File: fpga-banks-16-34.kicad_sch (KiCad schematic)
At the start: 20 parts, among them U3002 XC7K160T-FFG676, U9001 Oscillator_SMD_100MHz_ASFLMB, U9002 PCA9517A_TSSOP

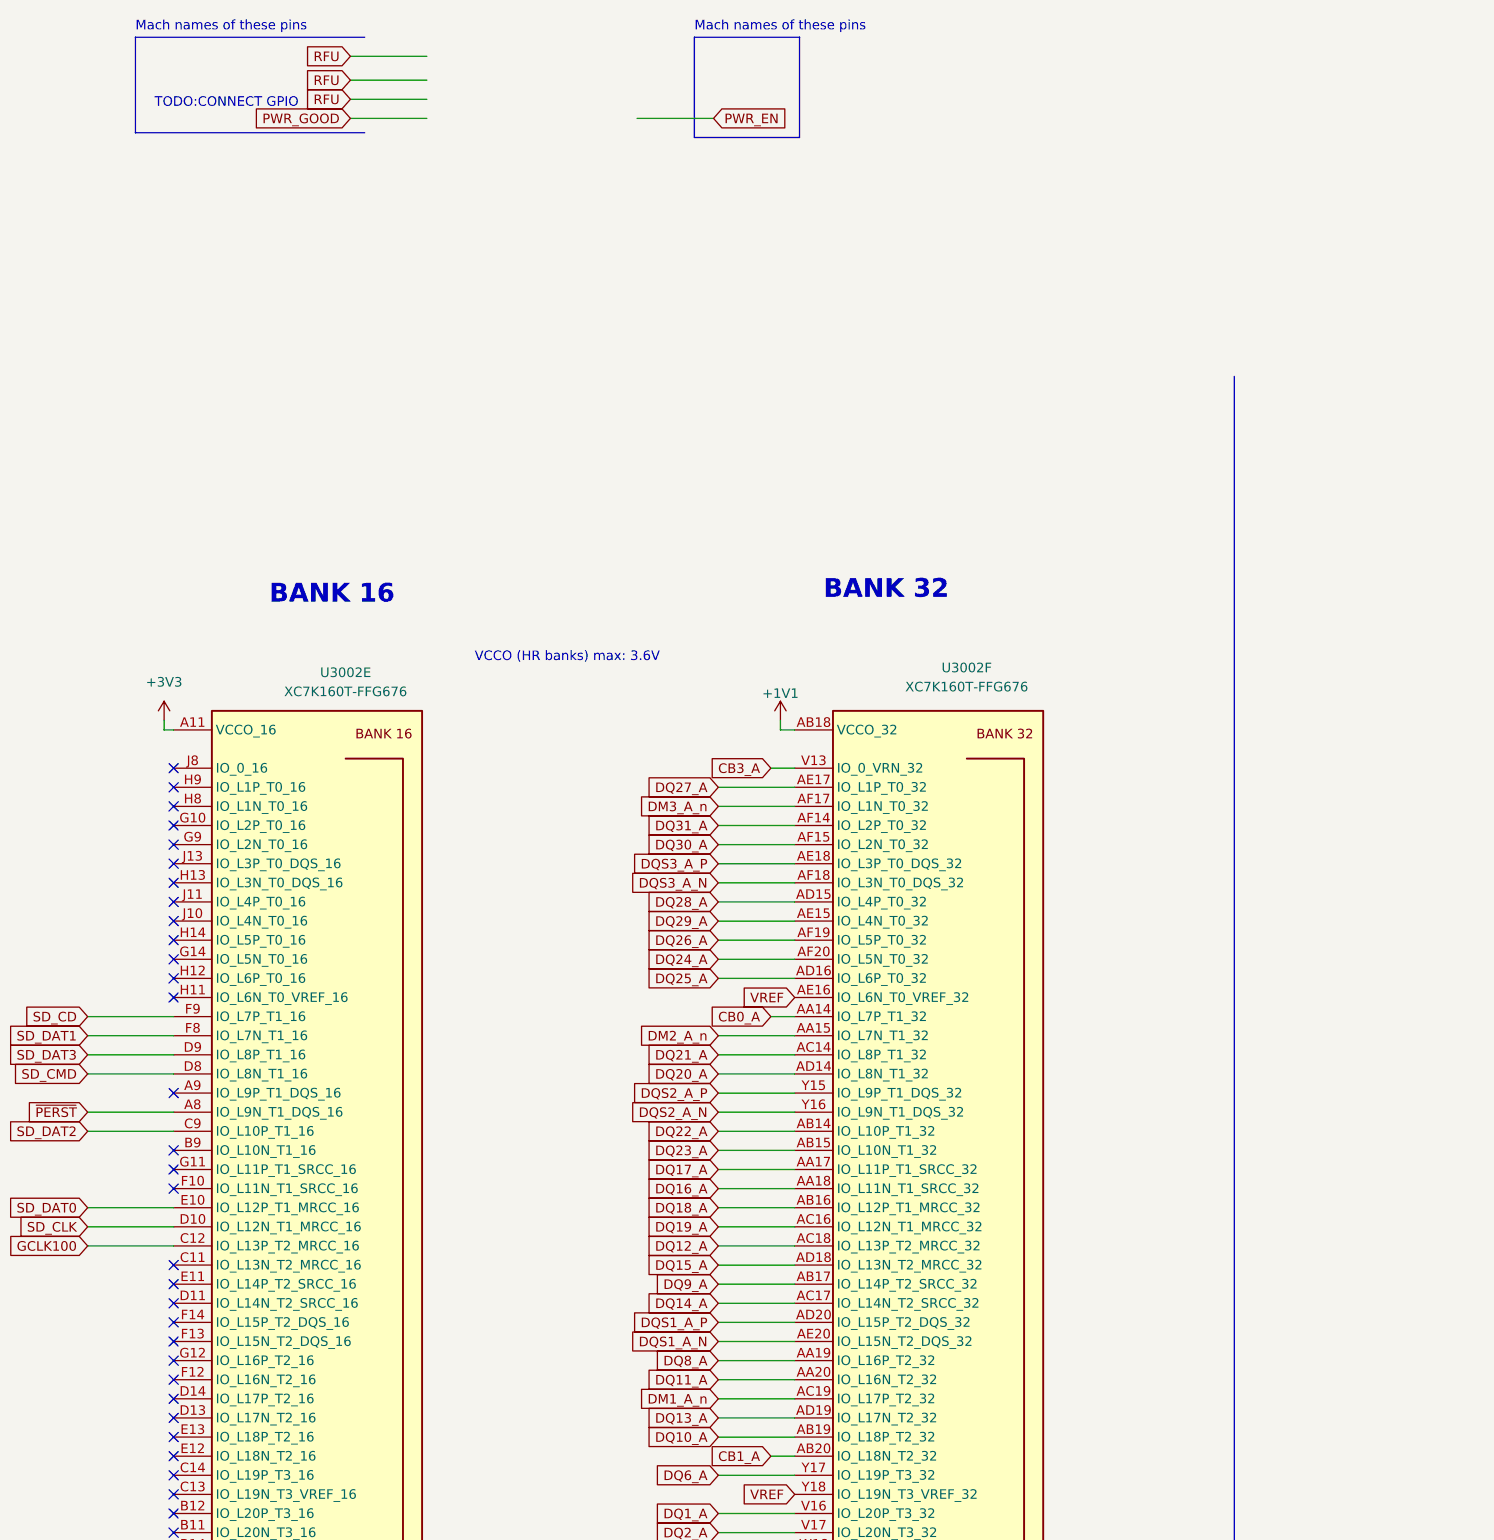
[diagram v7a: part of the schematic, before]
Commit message: Connect RFU, start improving interfaces and supply sheet, unify ESD protection
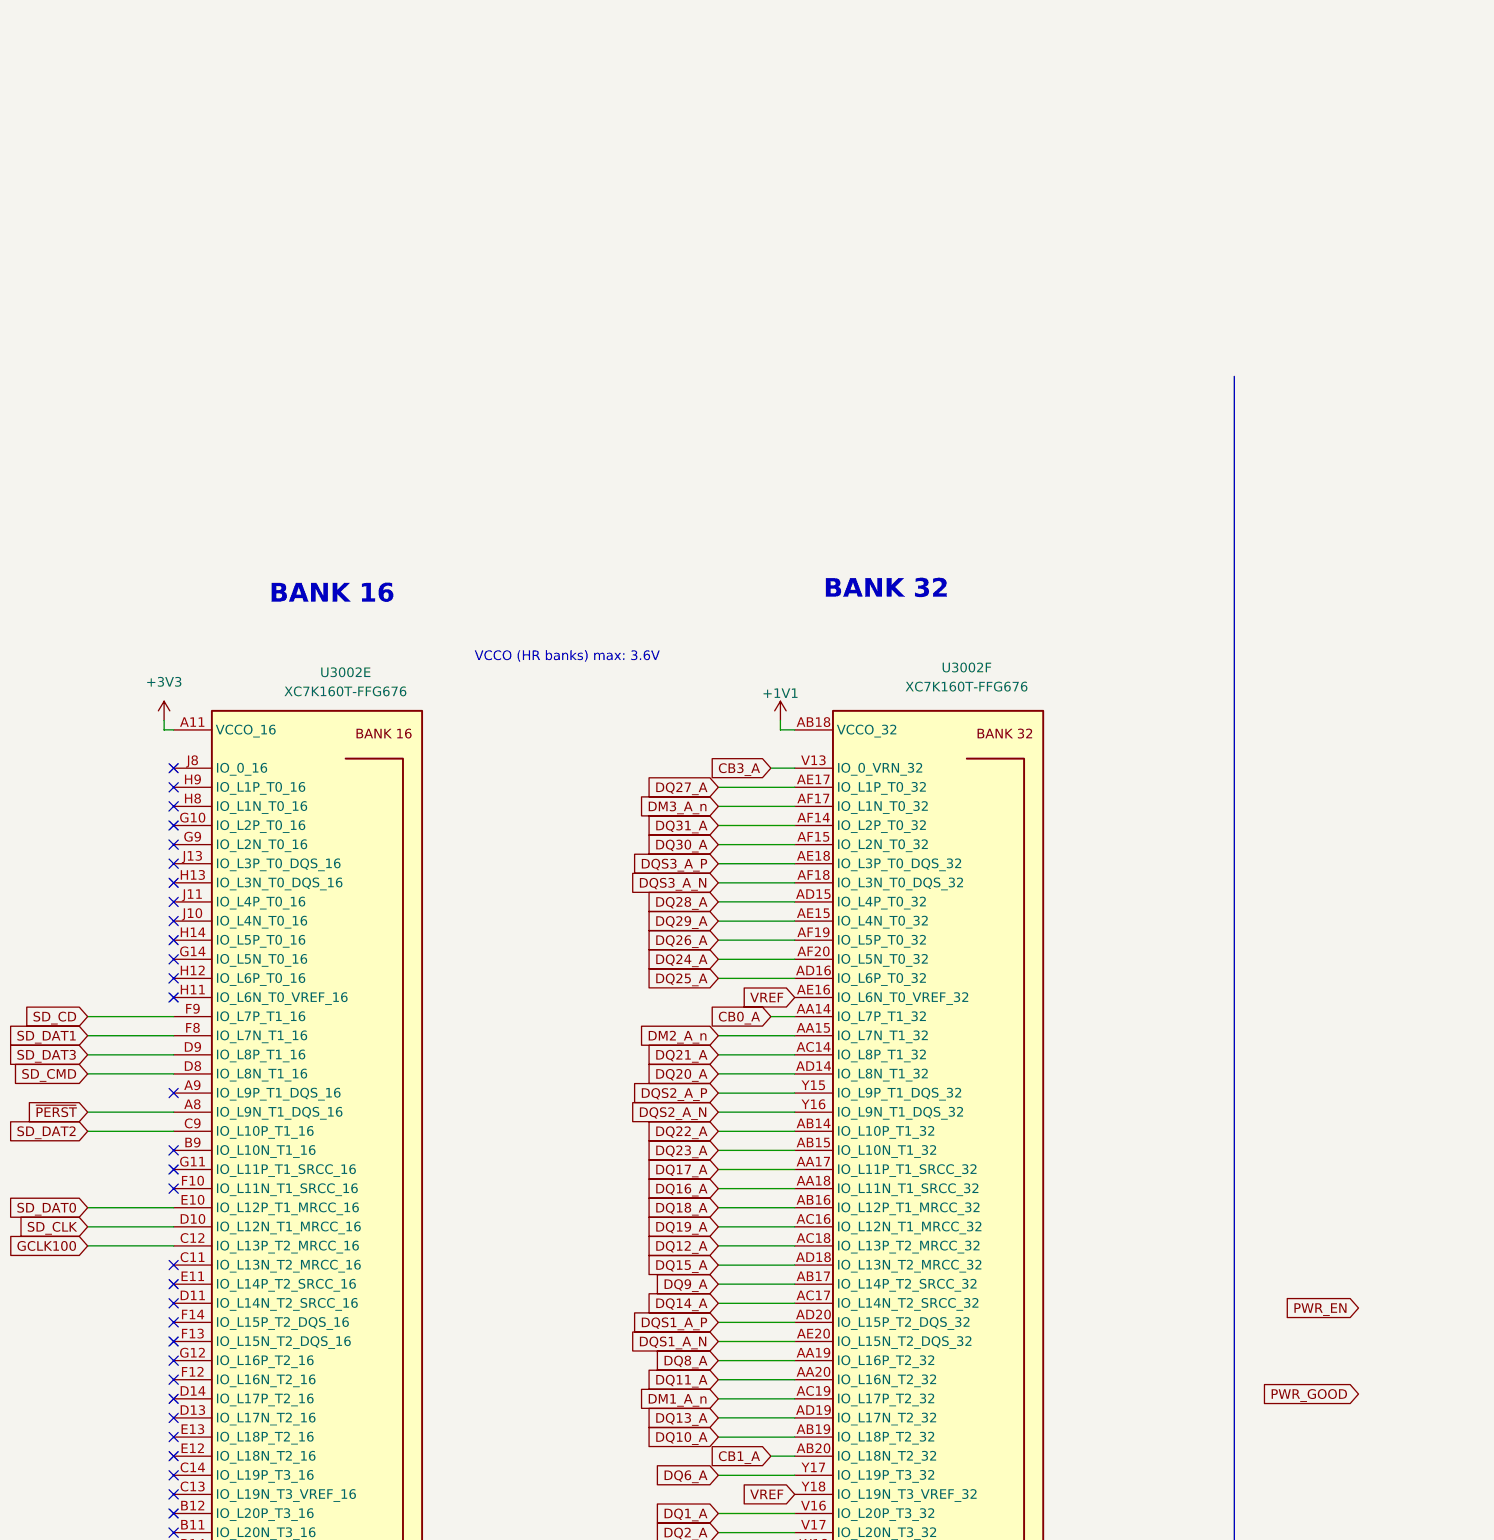
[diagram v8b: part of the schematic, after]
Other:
- note removed: "Mach names of these pins"
- note removed: "TODO:CONNECT GPIO"
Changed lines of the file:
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@@
     (stroke (width 0) (type default) (color 0 0 0 0))
   )
-  (polyline (pts (xy 50.8 -32.385) (xy 50.8 -19.685))
-    (stroke (width 0) (type default) (color 0 0 0 0))
-  )
   (wire (pts (xy 328.93 125.73) (xy 318.77 125.73))
     (stroke (width 0) (type default) (color 0 0 0 0))
@@
     (stroke (width 0) (type default) (color 0 0 0 0))
   )
-  (polyline (pts (xy 125.095 -32.385) (xy 139.065 -32.385))
-    (stroke (width 0) (type default) (color 0 0 0 0))
-  )
   (wire (pts (xy 44.45 113.03) (xy 55.88 113.03))
     (stroke (width 0) (type default) (color 0 0 0 0))
@@
     (stroke (width 0) (type default) (color 0 0 0 0))
   )
-  (wire (pts (xy 79.375 -29.845) (xy 89.535 -29.845))
-    (stroke (width 0) (type default) (color 0 0 0 0))
-  )
   (wire (pts (xy 318.77 138.43) (xy 328.93 138.43))
     (stroke (width 0) (type default) (color 0 0 0 0))
@@
     (stroke (width 0) (type default) (color 0 0 0 0))
   )
-  (polyline (pts (xy 125.095 -32.385) (xy 125.095 -19.05))
-    (stroke (width 0) (type default) (color 0 0 0 0))
-  )
   (wire (pts (xy 54.61 58.42) (xy 54.61 59.69))
     (stroke (width 0) (type default) (color 0 0 0 0))
@@
     (stroke (width 0) (type default) (color 0 0 0 0))
   )
-  (polyline (pts (xy 50.8 -19.685) (xy 81.28 -19.685))
-    (stroke (width 0) (type default) (color 0 0 0 0))
-  )
   (wire (pts (xy 238.125 252.73) (xy 241.935 252.73))
     (stroke (width 0) (type default) (color 0 0 0 0))
@@
     (stroke (width 0) (type default) (color 0 0 0 0))
   )
-  (wire (pts (xy 127.635 -21.59) (xy 117.475 -21.59))
-    (stroke (width 0) (type default) (color 0 0 0 0))
-  )
   (wire (pts (xy 214.63 263.525) (xy 227.33 263.525))
     (stroke (width 0) (type default) (color 0 0 0 0))
@@
     (stroke (width 0) (type default) (color 0 0 0 0))
   )
-  (wire (pts (xy 79.375 -21.59) (xy 89.535 -21.59))
-    (stroke (width 0) (type default) (color 0 0 0 0))
-  )
-  (wire (pts (xy 79.375 -24.13) (xy 89.535 -24.13))
-    (stroke (width 0) (type default) (color 0 0 0 0))
-  )
   (wire (pts (xy 248.92 135.89) (xy 259.08 135.89))
     (stroke (width 0) (type default) (color 0 0 0 0))
@@
     (stroke (width 0) (type default) (color 0 0 0 0))
   )
-  (wire (pts (xy 79.375 -26.67) (xy 89.535 -26.67))
-    (stroke (width 0) (type default) (color 0 0 0 0))
-  )
   (wire (pts (xy 44.45 125.73) (xy 55.88 125.73))
     (stroke (width 0) (type default) (color 0 0 0 0))
@@
     (stroke (width 0) (type default) (color 0 0 0 0))
   )
-  (polyline (pts (xy 81.28 -32.385) (xy 50.8 -32.385))
-    (stroke (width 0) (type default) (color 0 0 0 0))
-  )
   (wire (pts (xy 318.77 67.31) (xy 328.93 67.31))
     (stroke (width 0) (type default) (color 0 0 0 0))
@@
     (stroke (width 0) (type default) (color 0 0 0 0))
   )
-  (polyline (pts (xy 125.095 -19.05) (xy 139.065 -19.05))
-    (stroke (width 0) (type default) (color 0 0 0 0))
-  )
   (wire (pts (xy 318.77 186.69) (xy 328.93 186.69))
     (stroke (width 0) (type default) (color 0 0 0 0))
@@
     (stroke (width 0) (type default) (color 0 0 0 0))
   )
-  (polyline (pts (xy 139.065 -19.05) (xy 139.065 -32.385))
-    (stroke (width 0) (type default) (color 0 0 0 0))
-  )
   (wire (pts (xy 128.27 82.55) (xy 138.43 82.55))
     (stroke (width 0) (type default) (color 0 0 0 0))
@@
     (effects (font (size 1.27 1.27)) (justify left bottom))
   )
-  (text "Mach names of these pins" (at 125.095 -33.02 0)
-    (effects (font (size 1.27 1.27)) (justify left bottom))
-  )
   (text "VCCO (HP banks) max: 2.0V" (at 295.91 50.8 0)
     (effects (font (size 1.27 1.27)) (justify left bottom))
@@
     (effects (font (size 1.27 1.27)) (justify left bottom))
   )
-  (text "TODO:CONNECT GPIO" (at 53.34 -22.86 0)
-    (effects (font (size 1.27 1.27)) (justify left bottom))
-  )
   (text "BANK 32" (at 142.24 42.545 0)
     (effects (font (size 2.4892 2.4892) (thickness 0.4978) bold) (justify left bottom))
@@
     (effects (font (size 1.27 1.27)) (justify left bottom))
   )
-  (text "Mach names of these pins" (at 50.8 -33.02 0)
-    (effects (font (size 1.27 1.27)) (justify left bottom))
-  )
   (text "VREF" (at 304.165 227.965 0)
     (effects (font (size 2.4892 2.4892) (thickness 0.4978) bold) (justify left bottom))
@@
     )
   )
-  (global_label "PWR_GOOD" (shape input) (at 79.375 -21.59 180) (fields_autoplaced)
+  (global_label "PWR_GOOD" (shape input) (at 213.36 147.955 180) (fields_autoplaced)
     (effects (font (size 1.27 1.27)) (justify right))
-    (property "Intersheet References" "${INTERSHEET_REFS}" (id 0) (at 66.8908 -21.6694 0)
+    (property "Intersheet References" "${INTERSHEET_REFS}" (id 0) (at 200.8758 147.8756 0)
       (effects (font (size 1.27 1.27)) (justify right) hide)
     )
@@
     )
   )
-  (global_label "RFU" (shape input) (at 79.375 -24.13 180) (fields_autoplaced)
-    (effects (font (size 1.27 1.27)) (justify right))
-    (property "Intersheet References" "${INTERSHEET_REFS}" (id 0) (at 73.3618 -24.2094 0)
-      (effects (font (size 1.27 1.27)) (justify right) hide)
-    )
-  )
   (global_label "DQ4_A" (shape input) (at 128.27 173.99 180) (fields_autoplaced)
     (effects (font (size 1.27 1.27)) (justify right))
@@
     )
   )
-  (global_label "RFU" (shape input) (at 79.375 -29.845 180) (fields_autoplaced)
-    (effects (font (size 1.27 1.27)) (justify right))
-    (property "Intersheet References" "${INTERSHEET_REFS}" (id 0) (at 73.3618 -29.9244 0)
-      (effects (font (size 1.27 1.27)) (justify right) hide)
-    )
-  )
   (global_label "DQS_2_B_P" (shape input) (at 318.77 107.95 180) (fields_autoplaced)
     (effects (font (size 1.27 1.27)) (justify right))
@@
     )
   )
-  (global_label "PWR_EN" (shape input) (at 127.635 -21.59 0) (fields_autoplaced)
-    (effects (font (size 1.27 1.27)) (justify left))
-    (property "Intersheet References" "${INTERSHEET_REFS}" (id 0) (at 137.3978 -21.6694 0)
-      (effects (font (size 1.27 1.27)) (justify left) hide)
+  (global_label "PWR_EN" (shape input) (at 213.36 136.525 180) (fields_autoplaced)
+    (effects (font (size 1.27 1.27)) (justify right))
+    (property "Intersheet References" "${INTERSHEET_REFS}" (id 0) (at 203.5972 136.6044 0)
+      (effects (font (size 1.27 1.27)) (justify right) hide)
     )
   )
@@
       (effects (font (size 1.27 1.27)) (justify right) hide)
     )
-  )
-  (global_label "RFU" (shape input) (at 79.375 -26.67 180) (fields_autoplaced)
-    (effects (font (size 1.27 1.27)) (justify right))
-    (property "Intersheet References" "${INTERSHEET_REFS}" (id 0) (at 73.3618 -26.7494 0)
-      (effects (font (size 1.27 1.27)) (justify right) hide)
-    )
